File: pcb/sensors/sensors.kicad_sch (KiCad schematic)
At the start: 23 parts, among them J1 5V POWER, J2 USB-C FLASH, SW1 BOOT, SW2 RESET, U1 ESP32-S3-MINI-1U-N8, U2 AMS1117-3.3

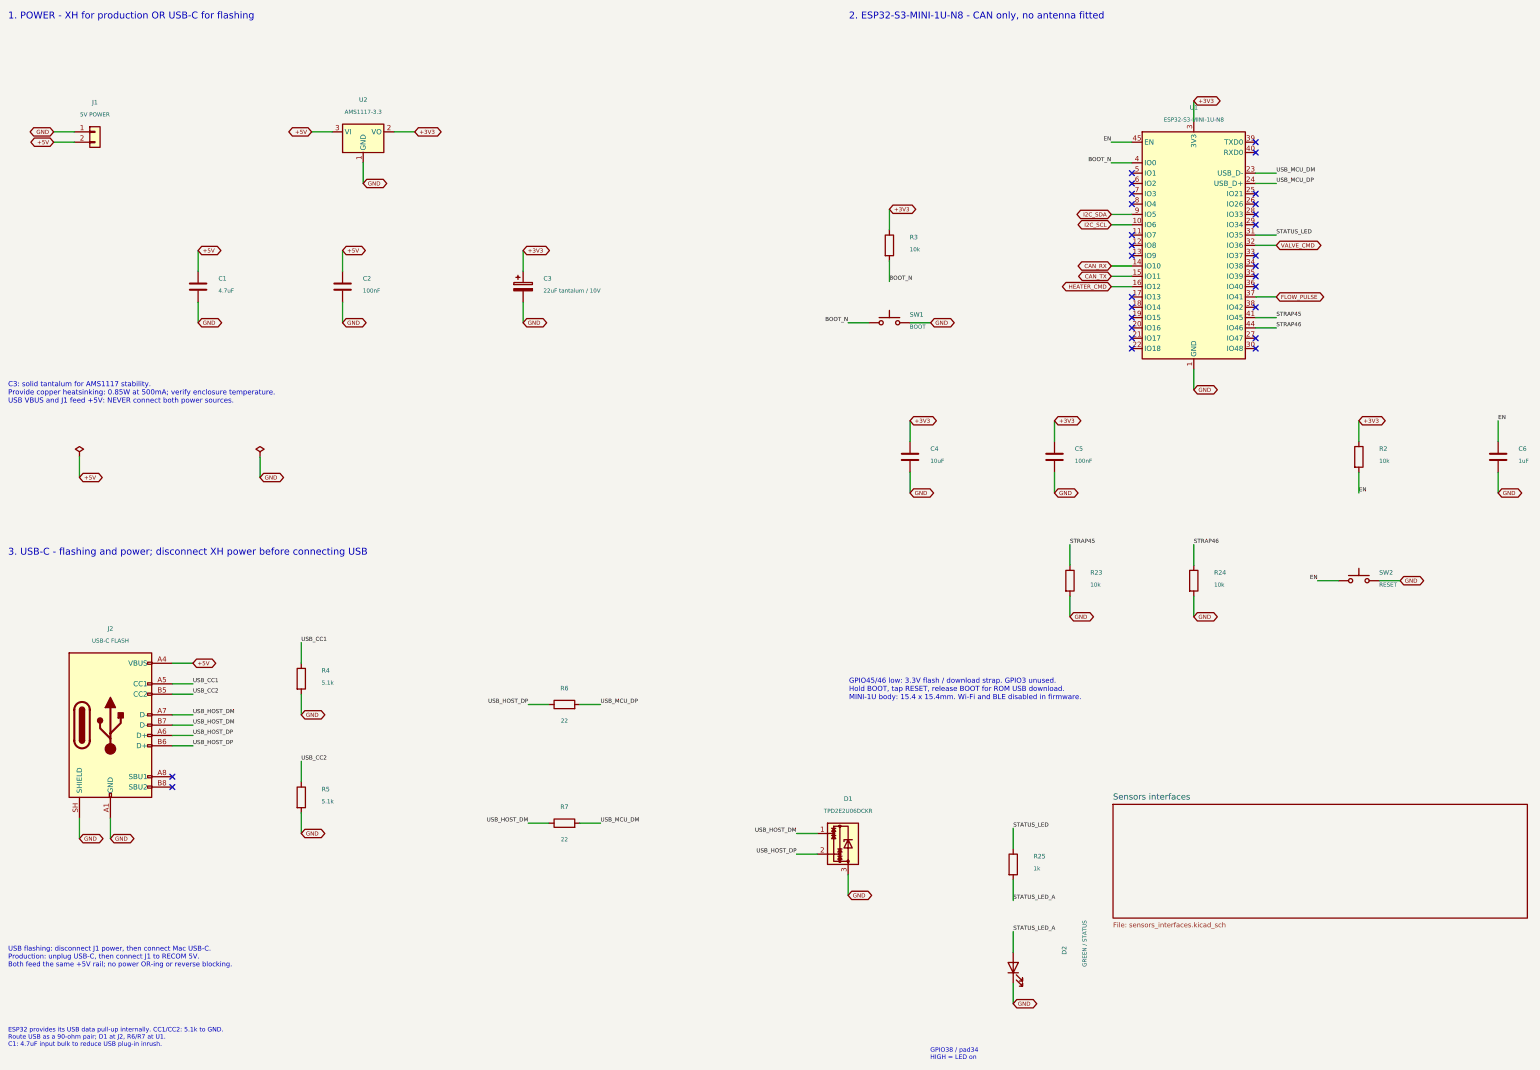
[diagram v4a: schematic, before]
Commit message: Replace sensors MINI controller with socketed XIAO ESP32-S3
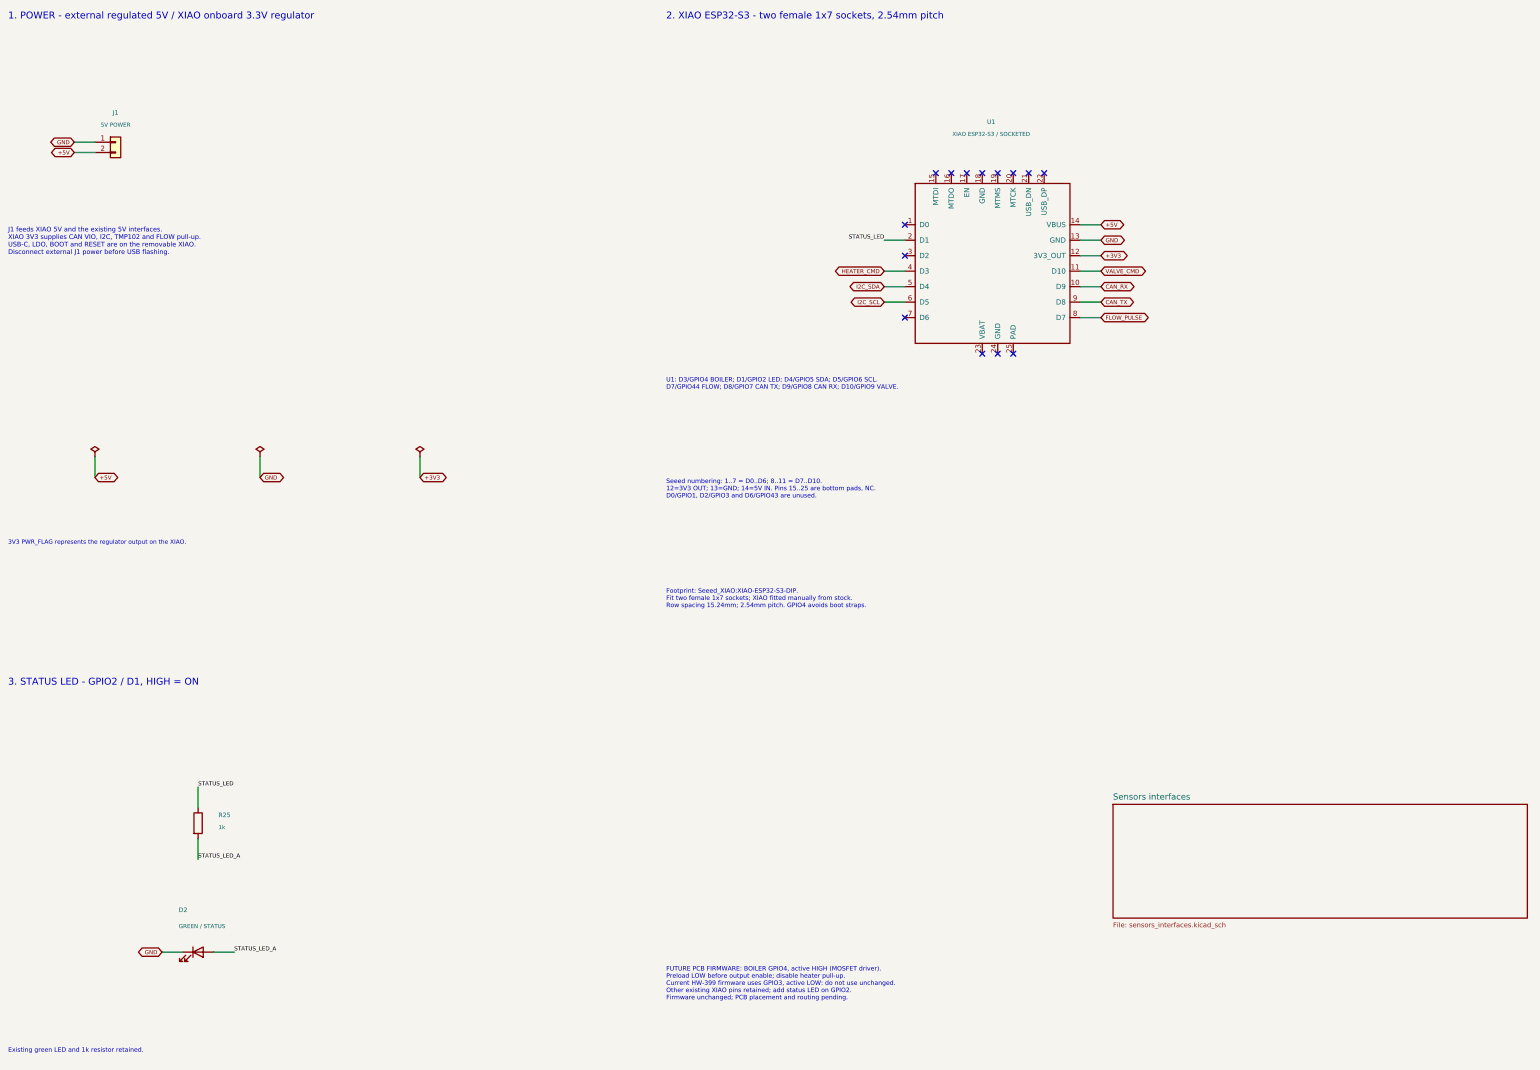
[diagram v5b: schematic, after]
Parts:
- removed C1: 4.7uF, Capacitor_SMD:C_0805_2012Metric, symbol Device:C
- removed C2, C5: 100nF, Capacitor_SMD:C_0603_1608Metric, symbol Device:C
- removed C3: 22uF tantalum / 10V, Capacitor_Tantalum_SMD:CP_EIA-3528-21_Kemet-B, symbol Device:C_Polarized
- removed C4: 10uF, Capacitor_SMD:C_0805_2012Metric, symbol Device:C
- removed C6: 1uF, Capacitor_SMD:C_0603_1608Metric, symbol Device:C
- removed D1: TPD2E2U06DCKR, Package_TO_SOT_SMD:SOT-323_SC-70, symbol Power_Protection:TPD2E2U06DCK
- removed J2: USB-C FLASH, Sensors_Local:USB_C_Receptacle_GCT_USB4105-xx-A_16P_TopMnt_Horizontal_RoundedGND, symbol Connector:USB_C_Receptacle_USB2.0_16P
- removed R2, R23, R24, R3: 10k, Resistor_SMD:R_0603_1608Metric, symbol Device:R
- removed R4, R5: 5.1k, Resistor_SMD:R_0603_1608Metric, symbol Device:R
- removed R6, R7: 22, Resistor_SMD:R_0603_1608Metric, symbol Device:R
- removed SW1: BOOT, Button_Switch_SMD:SW_SPST_TS-1088-xR020, symbol Switch:SW_Push
- removed SW2: RESET, Button_Switch_SMD:SW_SPST_TS-1088-xR020, symbol Switch:SW_Push
- removed U1: ESP32-S3-MINI-1U-N8, RF_Module:ESP32-S2-MINI-1U, symbol RF_Module:ESP32-S3-MINI-1U
- removed U2: AMS1117-3.3, Package_TO_SOT_SMD:SOT-223-3_TabPin2, symbol Regulator_Linear:AMS1117-3.3
- added U1: XIAO ESP32-S3 / SOCKETED, Seeed_XIAO:XIAO-ESP32-S3-DIP, symbol Seeed_Studio_XIAO_Series:XIAO-ESP32-S3-SMD
- D2: footprint LED_SMD:LED_0603_1608Metric -> LED_SMD:LED_0805_2012Metric; LCSC C2289 -> C2297; MPN KT-0603YG -> KT-0805G
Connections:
- net +3V3: now also U1.12 (3V3_OUT)
- net +5V: now also U1.14 (VBUS)
- net CAN_RX: now also U1.10 (D9)
- net CAN_TX: now also U1.9 (D8)
- net FLOW_PULSE: now also U1.8 (D7)
- net GND: now also U1.13 (GND)
- net HEATER_CMD: now also U1.4 (D3)
- net I2C_SCL: now also U1.6 (D5)
- net I2C_SDA: now also U1.5 (D4)
- net STATUS_LED: now also U1.2 (D1)
- net VALVE_CMD: now also U1.11 (D10)
- no-connect marks 28 -> 14
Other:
- note added: "1. POWER - external regulated 5V / XIAO onboard 3.3V regulator"
- note added: "2. XIAO ESP32-S3 - two female 1x7 sockets, 2.54mm pitch"
- note added: "3. STATUS LED - GPIO2 / D1, HIGH = ON"
- note added: "3V3 PWR_FLAG represents the regulator output on the XIAO."
- note added: "Existing green LED and 1k resistor retained."
- note added: "FUTURE PCB FIRMWARE: BOILER GPIO4, active HIGH (MOSFET driver). Preload LOW before output enable; disable heater pull-up. Current HW-399 firmware uses GPIO3, active LOW: do not use unchanged. Other existing XIAO pins retained; add status LED on GPIO2. Firmware unchanged; PCB placement and routing pending."
- note added: "Footprint: Seeed_XIAO:XIAO-ESP32-S3-DIP. Fit two female 1x7 sockets; XIAO fitted manually from stock. Row spacing 15.24mm; 2.54mm pitch. GPIO4 avoids boot straps."
- note added: "J1 feeds XIAO 5V and the existing 5V interfaces. XIAO 3V3 supplies CAN VIO, I2C, TMP102 and FLOW pull-up. USB-C, LDO, BOOT and RESET are on the removable XIAO. Disconnect external J1 power before USB flashing."
- note added: "Seeed numbering: 1..7 = D0..D6; 8..11 = D7..D10. 12=3V3 OUT; 13=GND; 14=5V IN. Pins 15..25 are bottom pads, NC. D0/GPIO1, D2/GPIO3 and D6/GPIO43 are unused."
- note added: "U1: D3/GPIO4 BOILER; D1/GPIO2 LED; D4/GPIO5 SDA; D5/GPIO6 SCL. D7/GPIO44 FLOW; D8/GPIO7 CAN TX; D9/GPIO8 CAN RX; D10/GPIO9 VALVE."
- note removed: "1. POWER - XH for production OR USB-C for flashing"
- note removed: "2. ESP32-S3-MINI-1U-N8 - CAN only, no antenna fitted"
- note removed: "3. USB-C - flashing and power; disconnect XH power before connecting USB"
- note removed: "C3: solid tantalum for AMS1117 stability. Provide copper heatsinking: 0.85W at 500mA; verify enclosure temperature. USB VBUS and J1 feed +5V: NEVER connect both power sources."
- note removed: "ESP32 provides its USB data pull-up internally. CC1/CC2: 5.1k to GND. Route USB as a 90-ohm pair; D1 at J2, R6/R7 at U1. C1: 4.7uF input bulk to reduce USB plug-in inrush."
- note removed: "GPIO38 / pad34 HIGH = LED on"
- note removed: "GPIO45/46 low: 3.3V flash / download strap. GPIO3 unused. Hold BOOT, tap RESET, release BOOT for ROM USB download. MINI-1U body: 15.4 x 15.4mm. Wi-Fi and BLE disabled in firmware."
- note removed: "USB flashing: disconnect J1 power, then connect Mac USB-C. Production: unplug USB-C, then connect J1 to RECOM 5V. Both feed the same +5V rail; no power OR-ing or reverse blocking."
- title: Sensors - power, ESP32-S3 and USB flashing -> Sensors - XIAO ESP32-S3 sockets and status LED
- moved on the sheet: D2, J1, R25
